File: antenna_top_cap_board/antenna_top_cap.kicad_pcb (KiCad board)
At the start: 4 copper layers, 100 x 100 mm, 61 parts, among them IC1 PCT2075DP,118, J1 Battery Charge Bypass, J10 USB_B_Micro, J11 USB_B_Micro, J12 BM04B-SRSS-TB(LF)(SN), J13 USB_B_Micro, J14 BM04B-SRSS-TB(LF)(SN), J15 USB_B_Micro, J16 BM04B-SRSS-TB(LF)(SN), J17 BM04B-SRSS-TB(LF)(SN)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

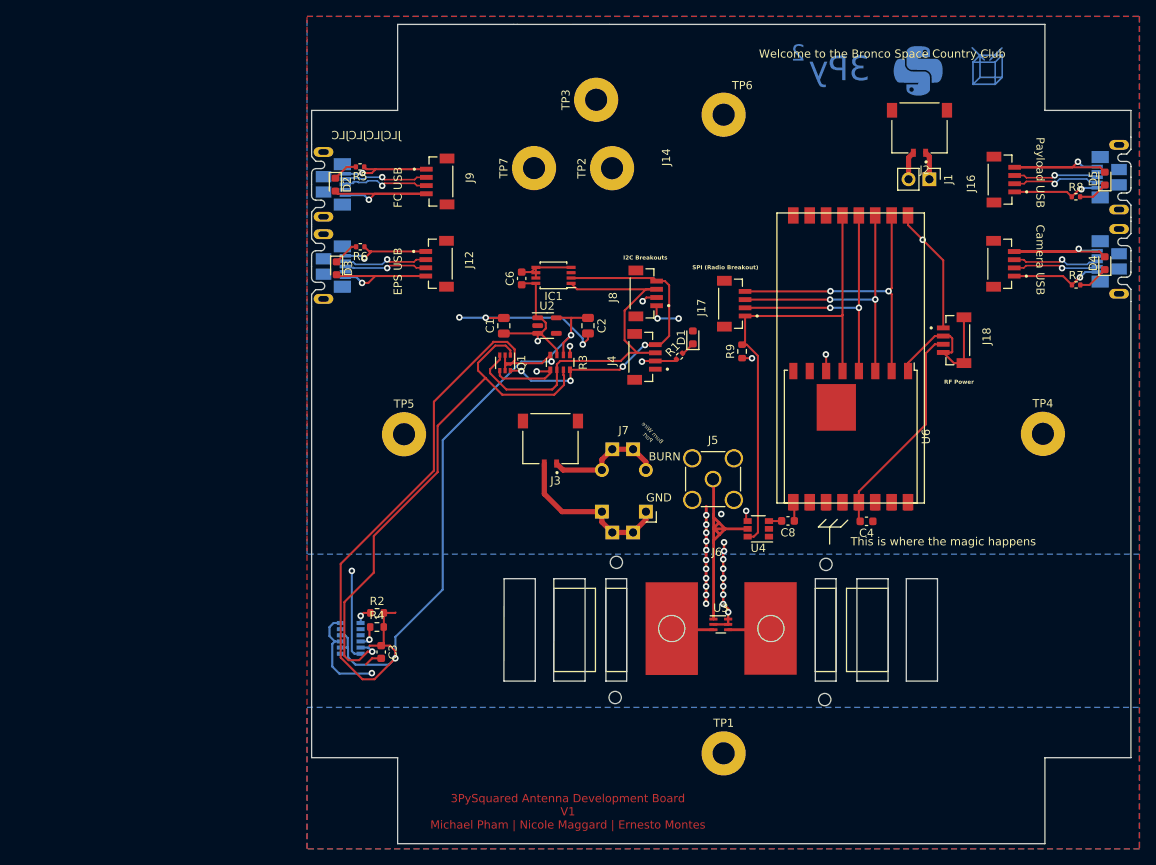
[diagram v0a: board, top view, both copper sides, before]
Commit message: Started wiring with 12-pos connector for V3b
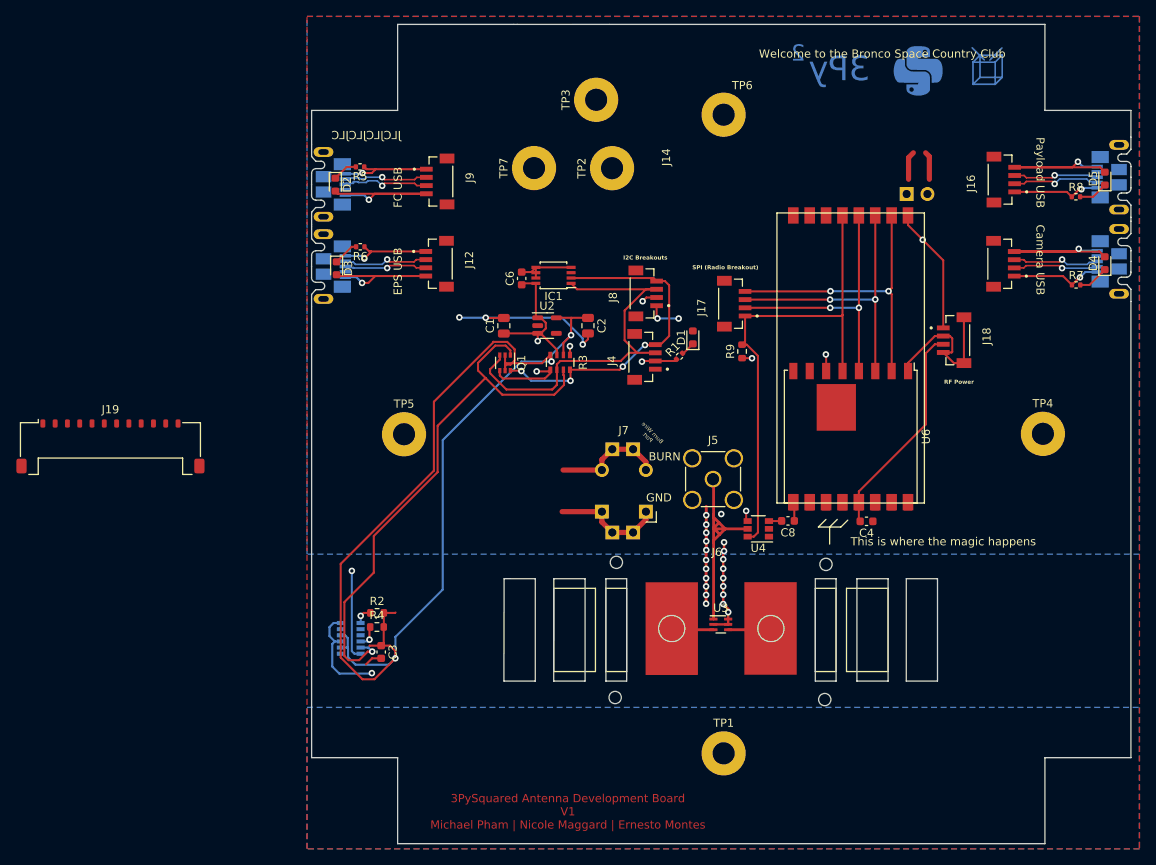
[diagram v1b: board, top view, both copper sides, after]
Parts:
- removed J2: Battery Charge Bypass, Picolock2Pos:MOLEX_504050-0291
- removed J3: Burn_Wire, Picolock2Pos:MOLEX_504050-0291
- removed REF**: VAL**, mainboard:board_info_block
- removed REF**: Val**, mainboard:XYZ_cubesat-top
- added J19: Z+_Cap_Connector, Connector_Molex:Molex_Pico-Lock_504050-1291_1x12-1MP_P1.50mm_Horizontal, F.Cu at (91.0, 113.7)
- J1: moved to B.Cu
- moved J1 3.31 mm to (188.2, 82.9)
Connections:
- J1 pad 1: /BATT_NEG -> Dir_Chrg_In
- J1 pad 2: /BATT_POS -> GND
- J7 pad 1: Net-(J3-Pin_1) -> GND
- J7 pad 2: Net-(J3-Pin_2) -> BURN
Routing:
- net Net-(J3-Pin_2): track 20.4 -> 0.00 mm
- net Net-(J3-Pin_1): track 15.2 -> 0.00 mm
- net GND: track 171.1 -> 185.2 mm
- net BURN: track 0.00 -> 13.7 mm
- net (no net): track 0.00 -> 6.89 mm
- net /BATT_POS: track 3.47 -> 0.00 mm
- net /BATT_NEG: track 3.42 -> 0.00 mm
- added copper zone on In1.Cu, net Dir_Chrg_In
- removed copper zone on In1.Cu, net /BATT_NEG

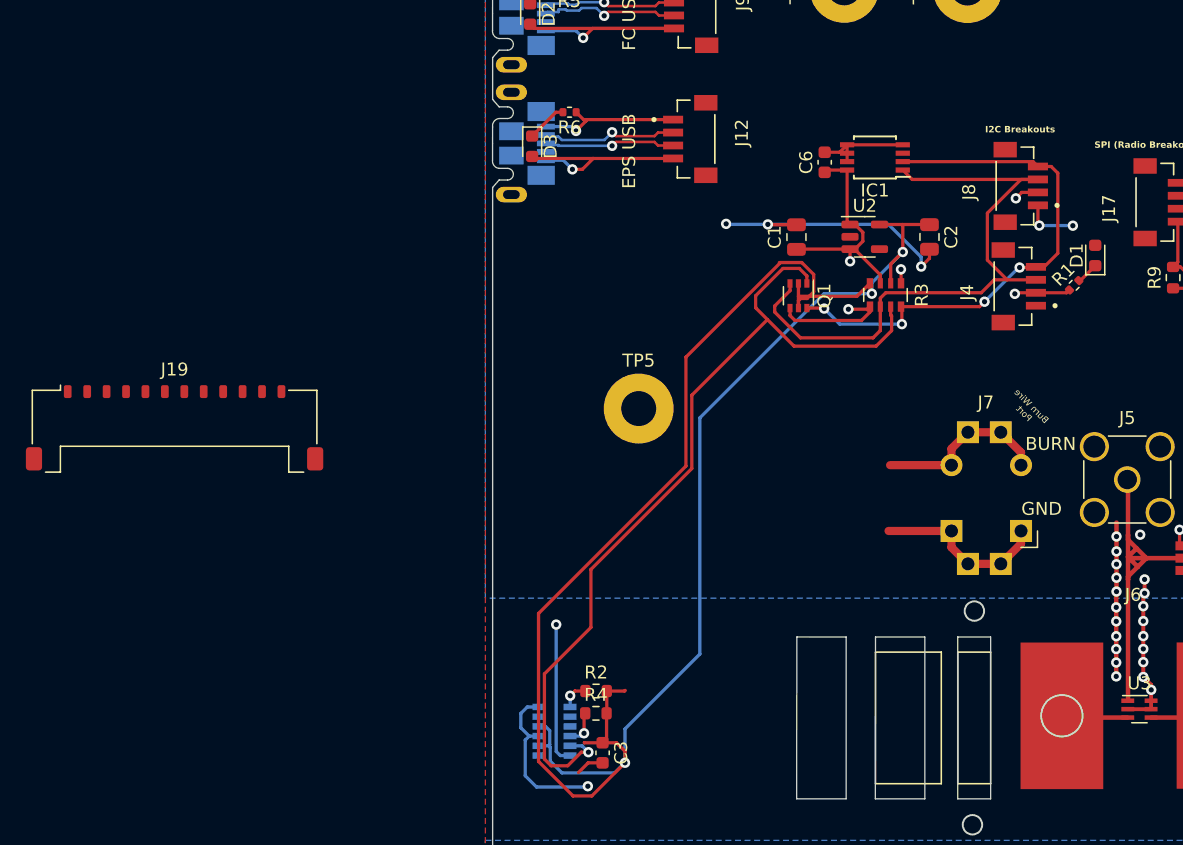
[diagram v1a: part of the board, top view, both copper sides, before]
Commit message: Scooted IC Layout
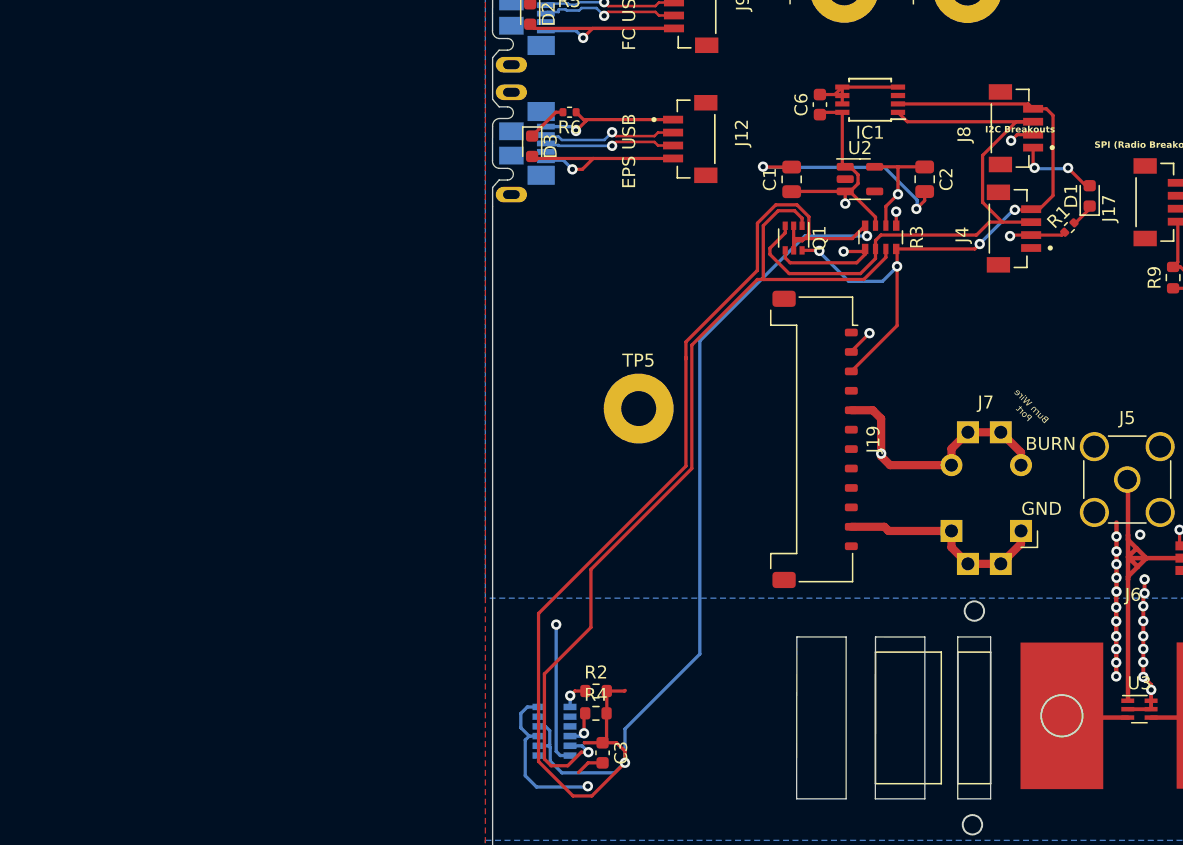
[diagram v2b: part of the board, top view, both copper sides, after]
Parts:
- moved J19 49.5 mm to (140.4, 114.6), turned to -90 degrees
- moved D1 4.62 mm to (161.6, 95.8)
- moved J4 4.47 mm to (154.6, 98.3)
- moved J8 4.47 mm to (154.8, 90.6)
- moved C1 4.47 mm to (138.6, 94.5)
- moved C2 4.47 mm to (148.9, 94.5)
- moved C6 4.47 mm to (140.8, 88.8)
- moved IC1 4.47 mm to (144.7, 88.4)
- moved R1 4.47 mm to (160.1, 98.3)
- moved R3 4.47 mm to (145.5, 99.0)
- moved U2 4.47 mm to (143.9, 94.5)
- moved Q1 4.47 mm to (138.8, 99.1)
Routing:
- net SCL1: track 41.6 -> 52.0 mm
- net GND: track 185.2 -> 190.7 mm
- net 2.8V: track 150.0 -> 155.1 mm
- net /SDA_3V: track 54.0 -> 58.3 mm
- net BURN: track 13.7 -> 16.7 mm
- net 3.3V: track 45.6 -> 47.6 mm, vias 8 -> 9
- net /SCL_3V: track 67.4 -> 69.3 mm
- net SDA1: track 48.5 -> 47.4 mm

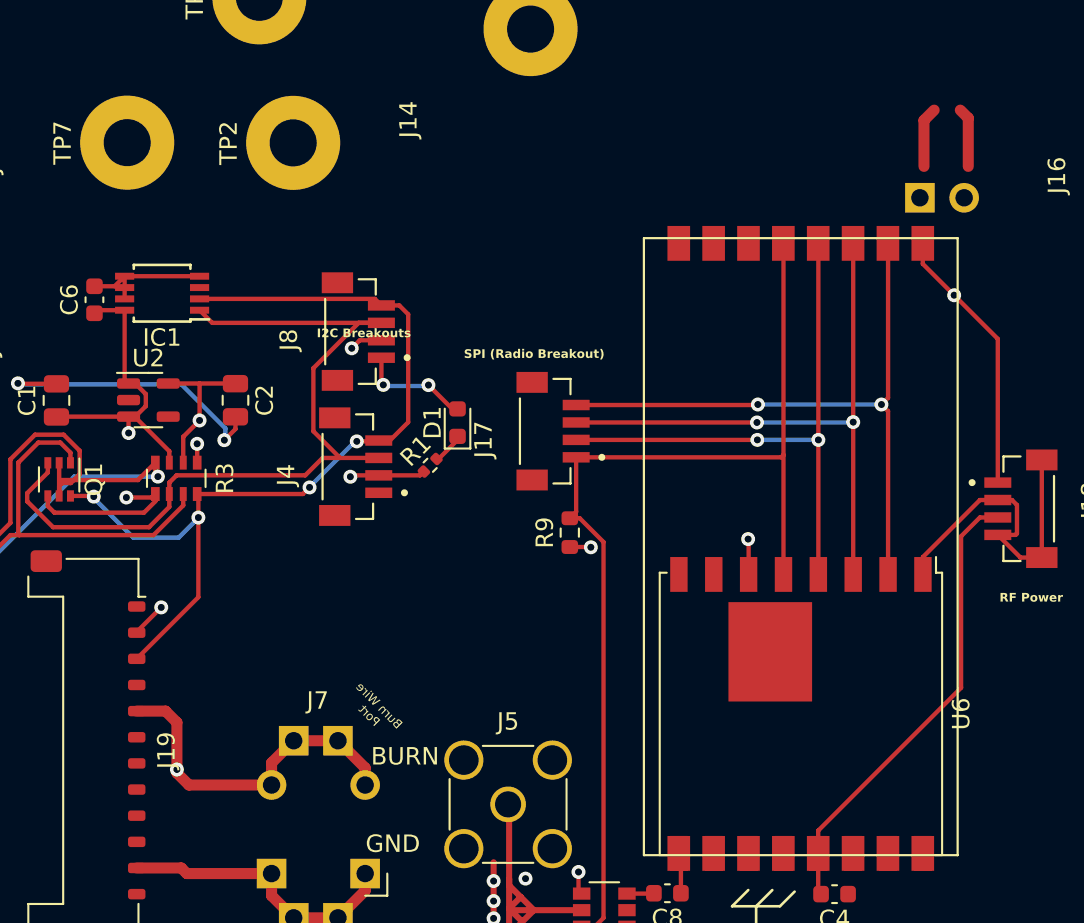
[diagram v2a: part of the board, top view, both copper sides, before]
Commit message: Update antenna_top_cap.kicad_pcb
Connected Direct Change to the 12 Pin Picolock
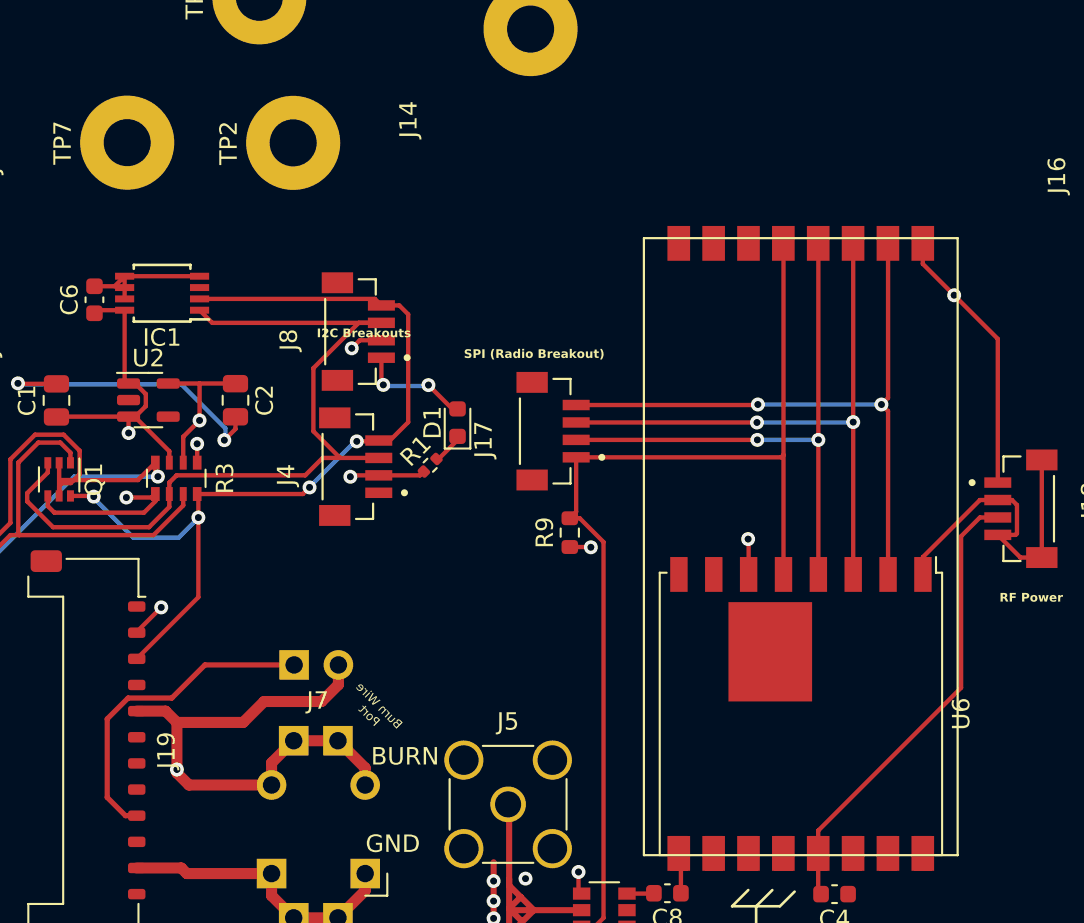
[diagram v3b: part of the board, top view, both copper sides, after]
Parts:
- moved J1 44.8 mm to (152.3, 109.7)
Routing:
- net Dir_Chrg_In: track 0.00 -> 18.6 mm
- net GND: track 190.7 -> 202.0 mm
- net (no net): track 6.89 -> 0.00 mm
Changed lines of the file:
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@@
 	(footprint "Connector_PinHeader_2.54mm:PinHeader_1x02_P2.54mm_Vertical"
 		(layer "B.Cu")
-		(at 188.1708 82.9194 -90)
+		(at 152.2708 109.7194 -90)
 		(descr "Through hole straight pin header, 1x02, 2.54mm pitch, single row")
 		(tags "Through hole pin header THT 1x02 2.54mm single row")
@@
 	)
 	(segment
-		(start 188.4058 81.1194)
-		(end 188.4058 78.474398)
-		(width 0.635)
-		(layer "F.Cu")
-		(net 0)
-	)
-	(segment
-		(start 190.9458 81.1194)
-		(end 190.9458 78.344402)
-		(width 0.635)
-		(layer "F.Cu")
-		(net 0)
-	)
-	(segment
-		(start 190.9458 78.344402)
-		(end 190.490798 77.8894)
-		(width 0.635)
-		(layer "F.Cu")
-		(net 0)
-	)
-	(segment
-		(start 188.4058 78.474398)
-		(end 188.990798 77.8894)
-		(width 0.635)
-		(layer "F.Cu")
-		(net 0)
-	)
-	(segment
 		(start 164.5858 135.4494)
 		(end 166.3858 135.4494)
@@
 	)
 	(segment
+		(start 154.8108 110.8544)
+		(end 154.8108 109.7194)
+		(width 0.635)
+		(layer "F.Cu")
+		(net 1)
+	)
+	(segment
 		(start 146.2358 116.6094)
 		(end 145.5458 115.9194)
@@
 	)
 	(segment
+		(start 153.8458 111.8194)
+		(end 154.8108 110.8544)
+		(width 0.635)
+		(layer "F.Cu")
+		(net 1)
+	)
+	(segment
 		(start 163.6958 127.5894)
 		(end 163.6958 132.9194)
@@
 	)
 	(segment
+		(start 145.5458 113.0194)
+		(end 149.3458 113.0194)
+		(width 0.635)
+		(layer "F.Cu")
+		(net 1)
+	)
+	(segment
+		(start 149.3458 113.0194)
+		(end 150.5458 111.8194)
+		(width 0.635)
+		(layer "F.Cu")
+		(net 1)
+	)
+	(segment
 		(start 145.5458 115.9194)
 		(end 145.5458 115.7194)
@@
 	)
 	(segment
+		(start 150.5458 111.8194)
+		(end 153.8458 111.8194)
+		(width 0.635)
+		(layer "F.Cu")
+		(net 1)
+	)
+	(segment
 		(start 145.5458 113.0194)
 		(end 144.8958 112.3694)
@@
 	)
 	(segment
+		(start 147.154788 109.7194)
+		(end 145.254788 111.6194)
+		(width 0.3)
+		(layer "F.Cu")
+		(net 6)
+	)
+	(segment
+		(start 152.2708 109.7194)
+		(end 147.154788 109.7194)
+		(width 0.3)
+		(layer "F.Cu")
+		(net 6)
+	)
+	(segment
+		(start 141.5458 117.3194)
+		(end 142.5958 118.3694)
+		(width 0.3)
+		(layer "F.Cu")
+		(net 6)
+	)
+	(segment
+		(start 141.5458 112.8194)
+		(end 141.5458 117.3194)
+		(width 0.3)
+		(layer "F.Cu")
+		(net 6)
+	)
+	(segment
+		(start 145.254788 111.6194)
+		(end 142.7458 111.6194)
+		(width 0.3)
+		(layer "F.Cu")
+		(net 6)
+	)
+	(segment
+		(start 142.7458 111.6194)
+		(end 141.5458 112.8194)
+		(width 0.3)
+		(layer "F.Cu")
+		(net 6)
+	)
+	(segment
+		(start 142.5958 118.3694)
+		(end 143.2408 118.3694)
+		(width 0.3)
+		(layer "F.Cu")
+		(net 6)
+	)
+	(segment

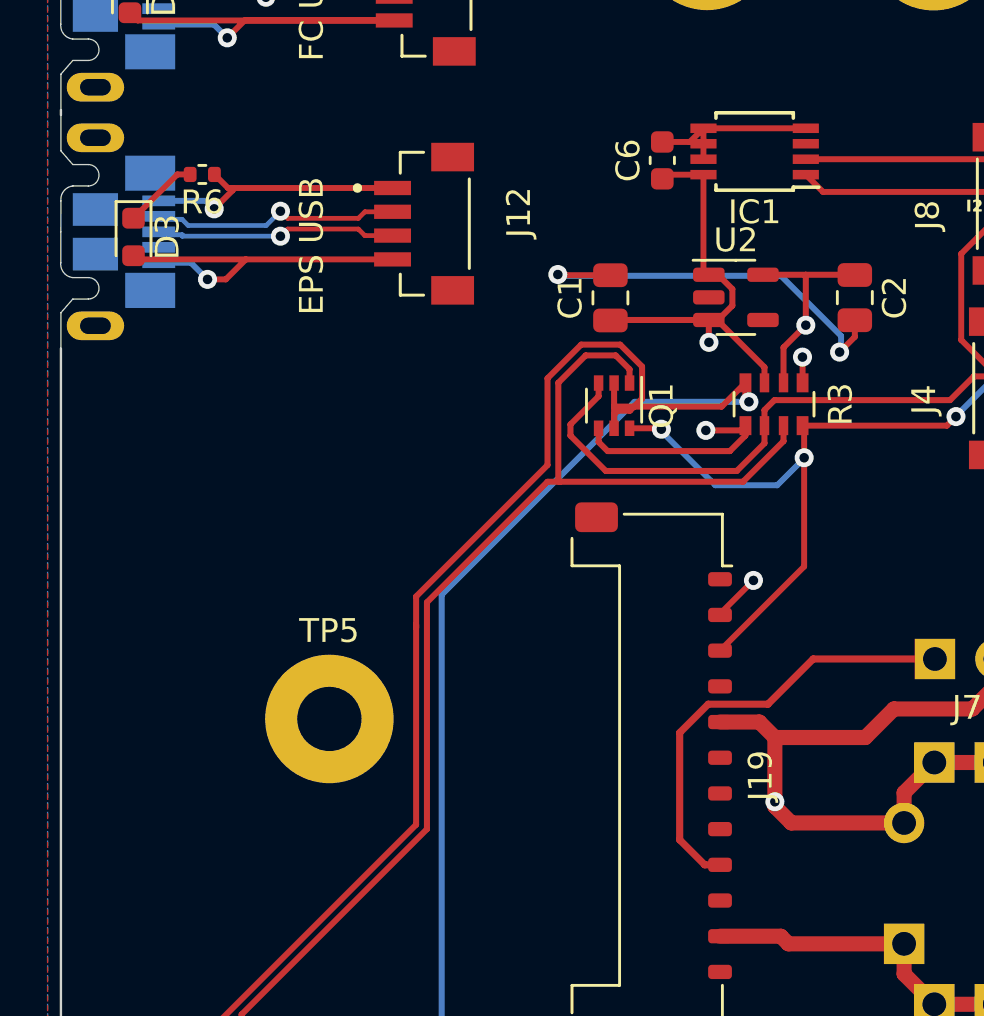
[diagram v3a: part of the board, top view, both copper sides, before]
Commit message: Connected USB Breakout
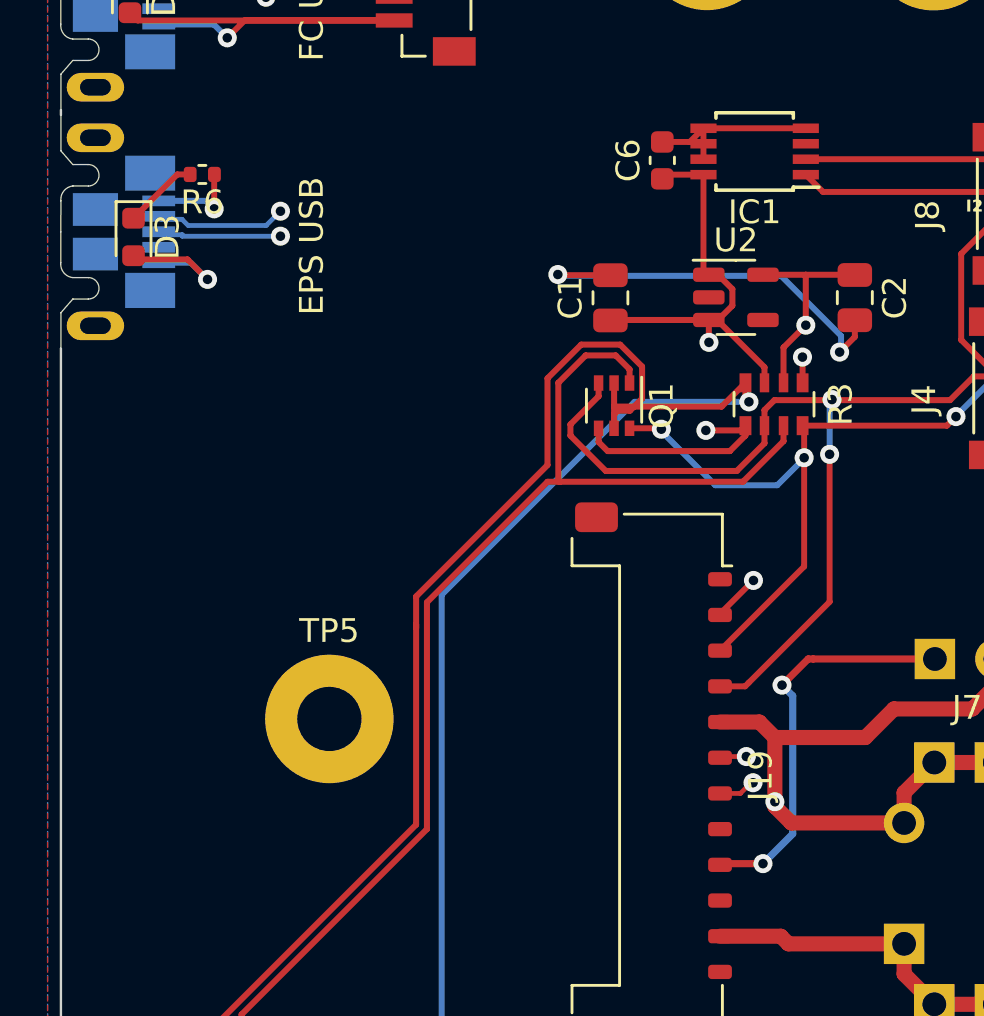
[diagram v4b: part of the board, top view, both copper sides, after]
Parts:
- removed J12: BM04B-SRSS-TB(LF)(SN), Antenna_board:JST_BM04B-SRSS-TB(LF)(SN)
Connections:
- J11 pad 2: /0d- -> USB_D-
- J11 pad 3: /0d+ -> USB_D+
- J18 pad 3: RF_VCC -> V_RF
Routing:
- net USB_D-: track 0.00 -> 39.7 mm, vias 0 -> 2
- net USB_D+: track 0.00 -> 36.6 mm, vias 0 -> 2
- net SDA1: track 47.4 -> 62.1 mm, vias 0 -> 2
- net /0d-: track 10.5 -> 0.00 mm, vias 1 -> 0
- net /0d+: track 10.2 -> 0.00 mm, vias 1 -> 0
- net GND: track 202.0 -> 192.6 mm
- net Net-(J11-VBUS): track 11.4 -> 3.92 mm
- net Dir_Chrg_In: track 18.6 -> 16.9 mm, vias 0 -> 2
